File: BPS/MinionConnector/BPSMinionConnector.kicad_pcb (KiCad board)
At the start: 2 copper layers, 85 x 66 mm, 44 parts, among them J1 TempConn2, J10 TempConn9, J11 TempConn10, J12 TempConn11, J13 TempConn12, J14 TempConn2, J15 TempConn13, J16 TempConn14, J17 TempConn15, J18 TempConn16, J2 TempConn3, J3 TempConn4, J4 TempConn5, J5 TempConn6, J6 TempConn7, J7 TempConn1, J8 TempConn8, J9 TempConn2

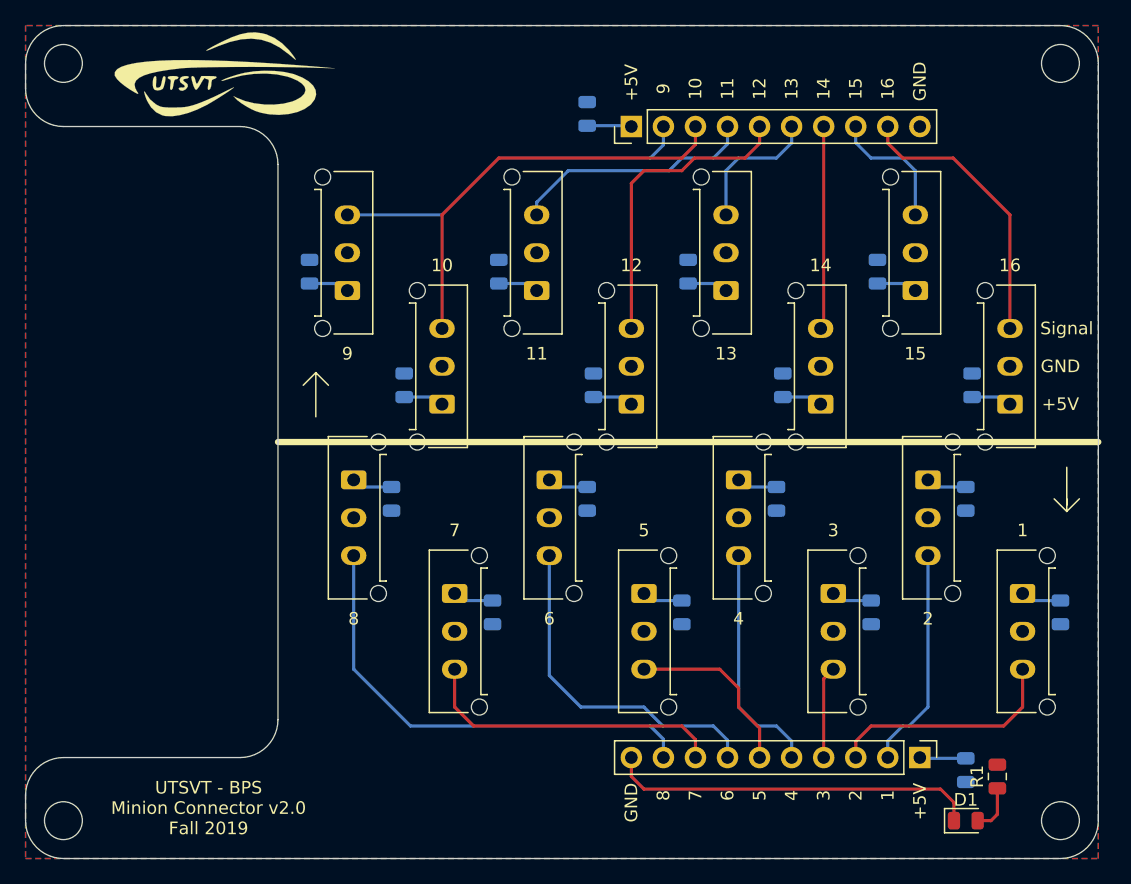
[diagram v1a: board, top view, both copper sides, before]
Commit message: Edits master board to not have temperature board pinouts.
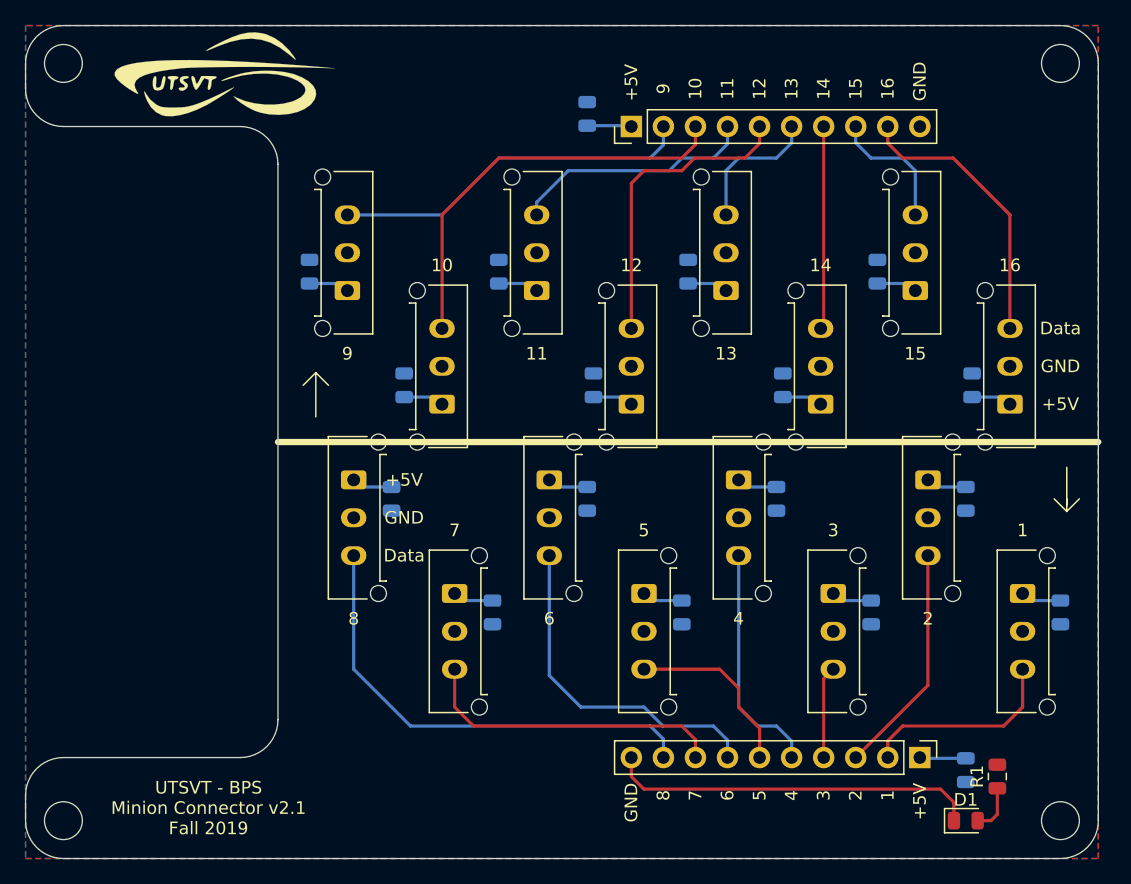
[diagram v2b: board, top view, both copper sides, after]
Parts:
- moved J1 11.7 mm to (171.5, 106.0)
- moved J7 11.7 mm to (179.0, 115.0)
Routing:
- net /TempSens1: track 17.6 -> 16.1 mm
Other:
- board text added: "Data"
- board text added: "UTSVT - BPS Minion Connector v2.1 Fall 2019"
- board text removed: "Signal"
- board text removed: "UTSVT - BPS Minion Connector v2.0 Fall 2019"
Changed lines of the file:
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@@
   (general
     (thickness 1.6)
-    (drawings 67)
-    (tracks 129)
+    (drawings 70)
+    (tracks 126)
     (zones 0)
     (modules 44)
@@
     (aux_axis_origin 0 0)
     (grid_origin 148 0)
-    (visible_elements FFFFFF7F)
+    (visible_elements 7FFFFFFF)
     (pcbplotparams
       (layerselection 0x010fc_ffffffff)
       (usegerberextensions false)
-      (usegerberattributes false)
+      (usegerberattributes true)
       (usegerberadvancedattributes false)
       (creategerberjobfile false)
@@
   )
   (module Connector_Molex:Molex_Micro-Fit_3.0_43650-0315_1x03_P3.00mm_Vertical (layer F.Cu)
-    (at 179 115 270)
+    (at 171.5 106 270)
     (descr "Molex Micro-Fit 3.0 Connector System, 43650-0315 (compatible alternatives: 43650-0316, 43650-0317), 3 Pins per row (http://www.molex.com/pdm_docs/sd/436500215_sd.pdf), generated with kicad-footprint-generator")
     (tags "connector Molex Micro-Fit_3.0 vertical")
@@
   )
   (module Connector_Molex:Molex_Micro-Fit_3.0_43650-0315_1x03_P3.00mm_Vertical (layer F.Cu)
-    (at 171.5 106 270)
+    (at 179 115 270)
     (descr "Molex Micro-Fit 3.0 Connector System, 43650-0315 (compatible alternatives: 43650-0316, 43650-0317), 3 Pins per row (http://www.molex.com/pdm_docs/sd/436500215_sd.pdf), generated with kicad-footprint-generator")
     (tags "connector Molex Micro-Fit_3.0 vertical")
@@
     )
   )
+  (gr_text +5V (at 130 106) (layer F.SilkS)
+    (effects (font (size 1 1) (thickness 0.15)))
+  )
+  (gr_text GND (at 130 109) (layer F.SilkS)
+    (effects (font (size 1 1) (thickness 0.15)))
+  )
+  (gr_text Data (at 130 112) (layer F.SilkS)
+    (effects (font (size 1 1) (thickness 0.15)))
+  )
+  (gr_text 1 (at 179 110) (layer F.SilkS)
+    (effects (font (size 1 1) (thickness 0.15)))
+  )
+  (gr_arc (start 117 125) (end 117 128) (angle -90) (layer Edge.Cuts) (width 0.05))
   (gr_text "Why you turn me over???" (at 115.5 74) (layer B.SilkS)
     (effects (font (size 1 1) (thickness 0.15)) (justify mirror))
   )
-  (gr_text Signal (at 182.5 94) (layer F.SilkS)
+  (gr_text Data (at 182 94) (layer F.SilkS)
     (effects (font (size 1 1) (thickness 0.15)))
   )
@@
     (effects (font (size 1 1) (thickness 0.15)))
   )
-  (gr_text 1 (at 179 110) (layer F.SilkS)
-    (effects (font (size 1 1) (thickness 0.15)))
-  )
   (gr_text 16 (at 178 89) (layer F.SilkS)
     (effects (font (size 1 1) (thickness 0.15)))
@@
     (effects (font (size 1 1) (thickness 0.15)))
   )
-  (gr_text "10\n" (at 133 89) (layer F.SilkS)
+  (gr_text 10 (at 133 89) (layer F.SilkS)
     (effects (font (size 1 1) (thickness 0.15)))
   )
@@
   (gr_line (start 123 97.5) (end 122 98.5) (layer F.SilkS) (width 0.12))
   (gr_line (start 123 101) (end 123 97.5) (layer F.SilkS) (width 0.12))
-  (gr_text "UTSVT - BPS\nMinion Connector v2.0\nFall 2019" (at 114.5 132) (layer F.SilkS)
+  (gr_text "UTSVT - BPS\nMinion Connector v2.1\nFall 2019" (at 114.5 132) (layer F.SilkS)
     (effects (font (size 1 1) (thickness 0.15)))
   )
@@
     (effects (font (size 1 1) (thickness 0.15)))
   )
-  (gr_text "1\n" (at 168.32 131 90) (layer F.SilkS)
+  (gr_text 1 (at 168.32 131 90) (layer F.SilkS)
     (effects (font (size 1 1) (thickness 0.15)))
   )
@@
   (gr_line (start 100 73) (end 100 75) (layer Edge.Cuts) (width 0.05))
   (gr_line (start 120 125) (end 120 81) (layer Edge.Cuts) (width 0.05))
-  (gr_arc (start 117 125) (end 117 128) (angle -90) (layer Edge.Cuts) (width 0.05))
   (gr_line (start 103 128) (end 117 128) (layer Edge.Cuts) (width 0.05))
   (dimension 33 (width 0.15) (layer Dwgs.User)
@@
   (segment (start 148 128) (end 148 129.5) (width 0.25) (layer F.Cu) (net 2))
   (segment (start 148 129.5) (end 149 130.5) (width 0.25) (layer F.Cu) (net 2))
-  (segment (start 179 121) (end 179 124) (width 0.25) (layer F.Cu) (net 3))
-  (segment (start 179 124) (end 177.5 125.5) (width 0.25) (layer F.Cu) (net 3))
-  (segment (start 177.5 125.5) (end 167 125.5) (width 0.25) (layer F.Cu) (net 3))
-  (segment (start 165.78 126.72) (end 165.78 128) (width 0.25) (layer F.Cu) (net 3))
-  (segment (start 167 125.5) (end 165.78 126.72) (width 0.25) (layer F.Cu) (net 3))
+  (segment (start 171.5 122.28) (end 165.78 128) (width 0.25) (layer F.Cu) (net 3))
+  (segment (start 171.5 112) (end 171.5 122.28) (width 0.25) (layer F.Cu) (net 3))
   (segment (start 163.24 121.76) (end 164 121) (width 0.25) (layer F.Cu) (net 4))
   (segment (start 163.24 128) (end 163.24 121.76) (width 0.25) (layer F.Cu) (net 4))
@@
   (segment (start 153.08 126.58) (end 153.08 128) (width 0.25) (layer F.Cu) (net 8))
   (segment (start 152 125.5) (end 153.08 126.58) (width 0.25) (layer F.Cu) (net 8))
-  (segment (start 168.32 128) (end 168.32 126.68) (width 0.25) (layer B.Cu) (net 9))
-  (segment (start 168.32 126.68) (end 169.5 125.5) (width 0.25) (layer B.Cu) (net 9))
-  (segment (start 169.5 125.5) (end 170 125.5) (width 0.25) (layer B.Cu) (net 9))
-  (segment (start 170 125.5) (end 171.5 124) (width 0.25) (layer B.Cu) (net 9))
-  (segment (start 171.5 124) (end 171.5 112) (width 0.25) (layer B.Cu) (net 9))
+  (segment (start 168.32 128) (end 168.32 126.68) (width 0.25) (layer F.Cu) (net 9))
+  (segment (start 168.32 126.68) (end 169.5 125.5) (width 0.25) (layer F.Cu) (net 9))
+  (segment (start 169.5 125.5) (end 177.5 125.5) (width 0.25) (layer F.Cu) (net 9))
+  (segment (start 179 124) (end 179 121) (width 0.25) (layer F.Cu) (net 9))
+  (segment (start 177.5 125.5) (end 179 124) (width 0.25) (layer F.Cu) (net 9))
   (segment (start 150.54 126.54) (end 150.54 128) (width 0.25) (layer B.Cu) (net 10))
   (segment (start 149.5 125.5) (end 150.54 126.54) (width 0.25) (layer B.Cu) (net 10))
